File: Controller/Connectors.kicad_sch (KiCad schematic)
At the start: 24 parts, among them J10 Servo, J11 Servo, J12 Thruster, J14 I2C, J15 I2C, J16 UART1, J17 UART2, J18 SPI1, J19 SPI2, J20 Interrupt, J21 Interrupt, J22 Interrupt, J4 Servo, J5 Servo, J6 Servo, J7 Servo, J8 Servo, J9 Servo

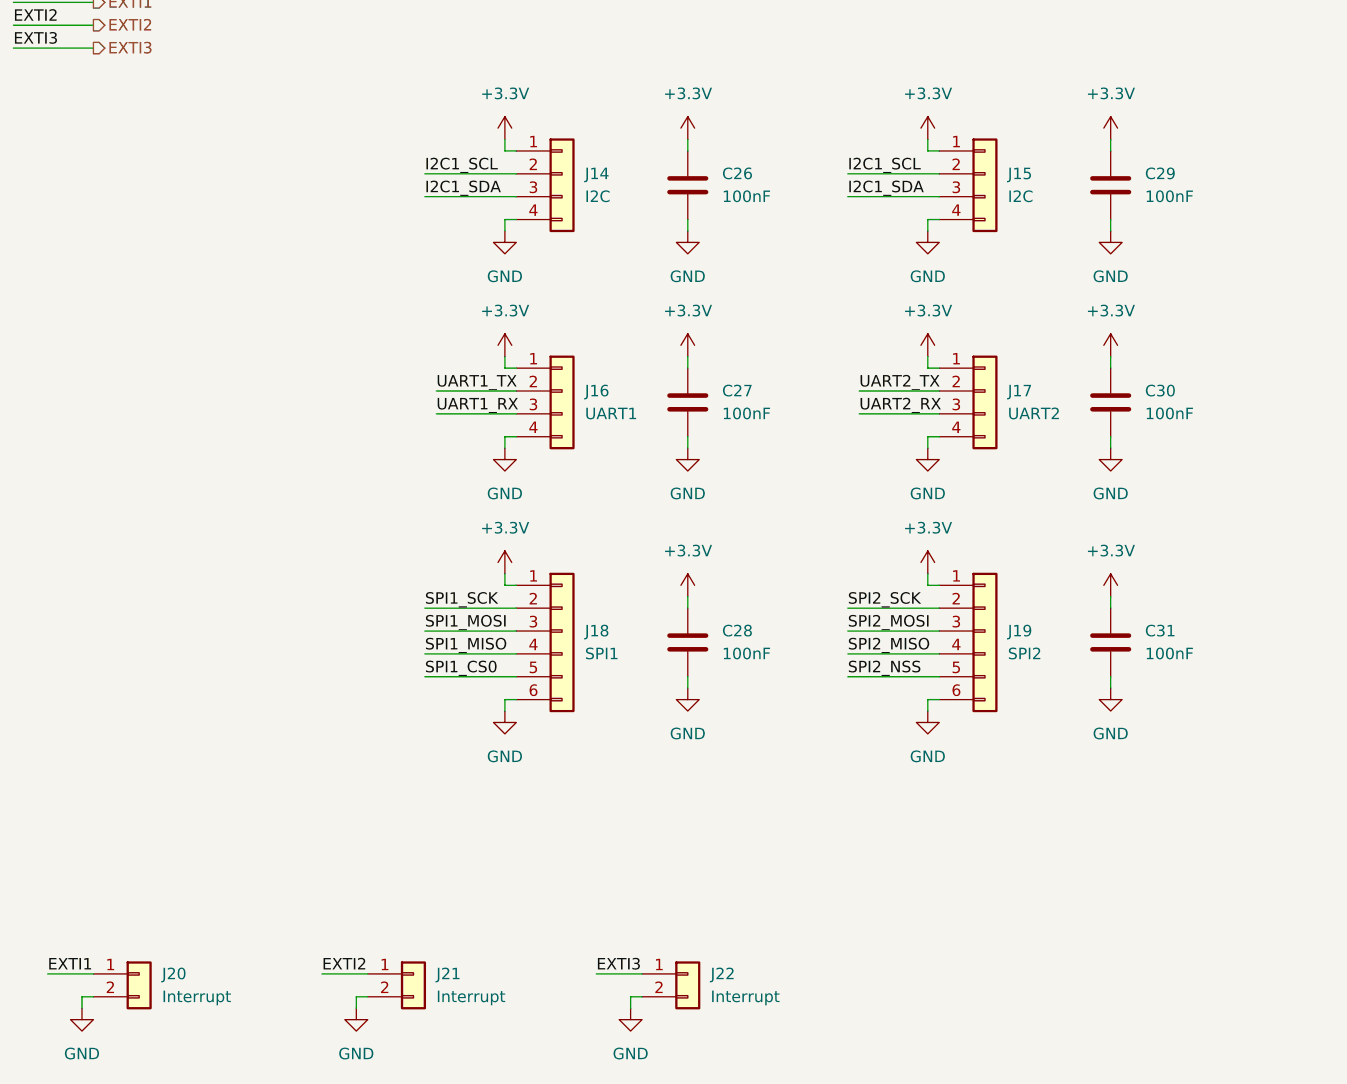
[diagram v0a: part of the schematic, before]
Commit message: Re-number components in controller schematic
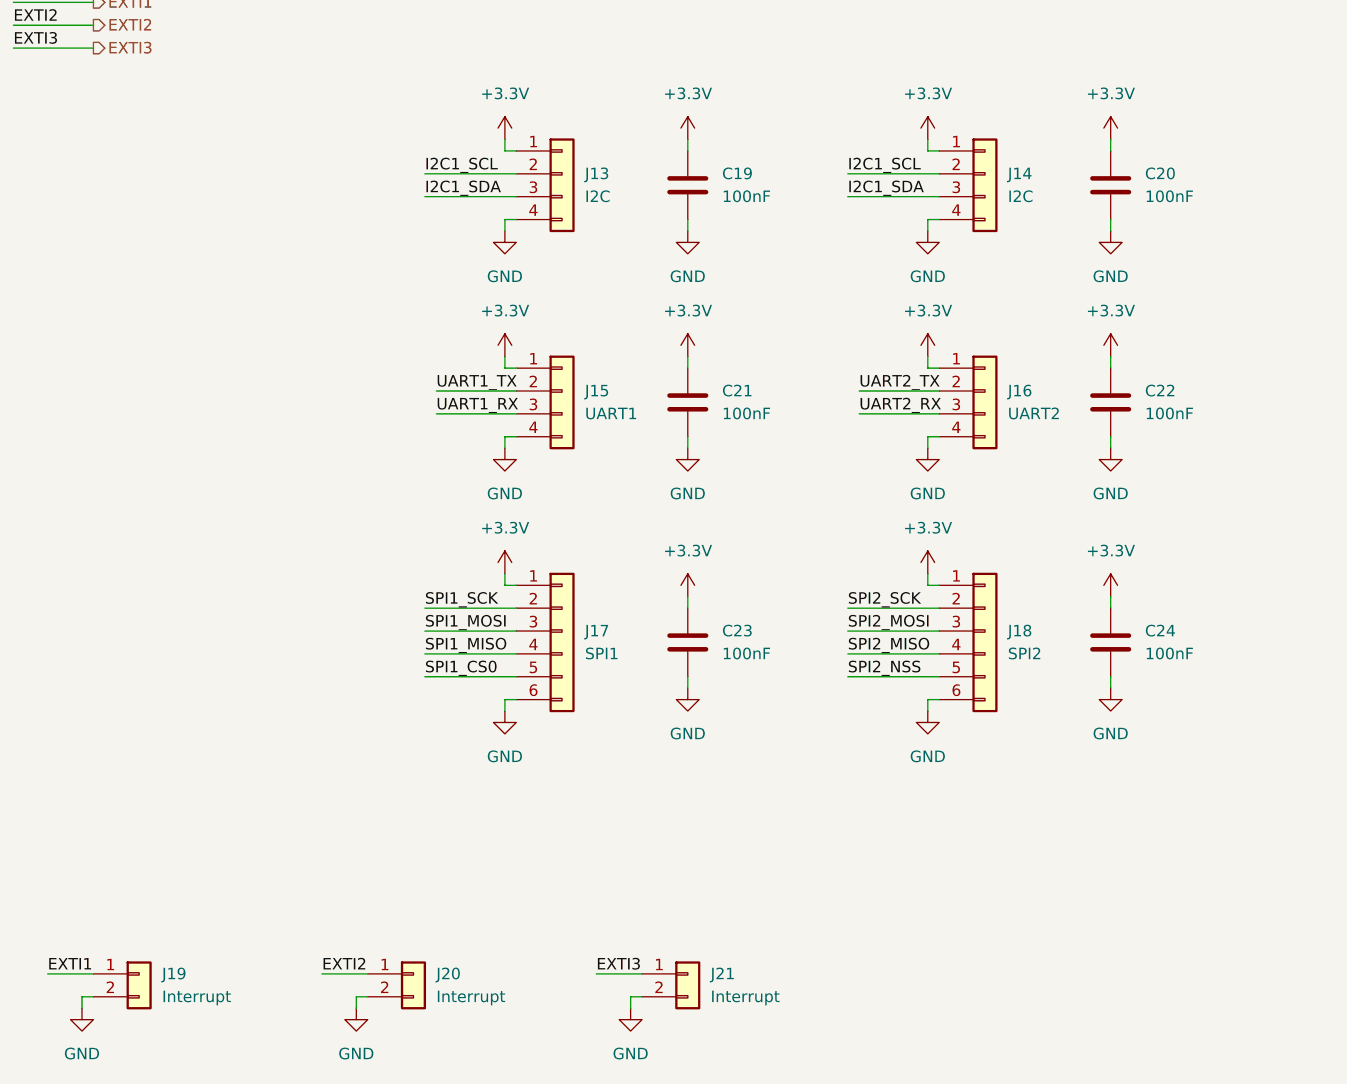
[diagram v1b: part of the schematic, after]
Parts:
- renumbered C26 to C19, C29 to C20, C27 to C21, C30 to C22, C28 to C23, C31 to C24, J14 to J13, J15 to J14, J16 to J15, J17 to J16, J18 to J17, J19 to J18, J20 to J19, J21 to J20, J22 to J21

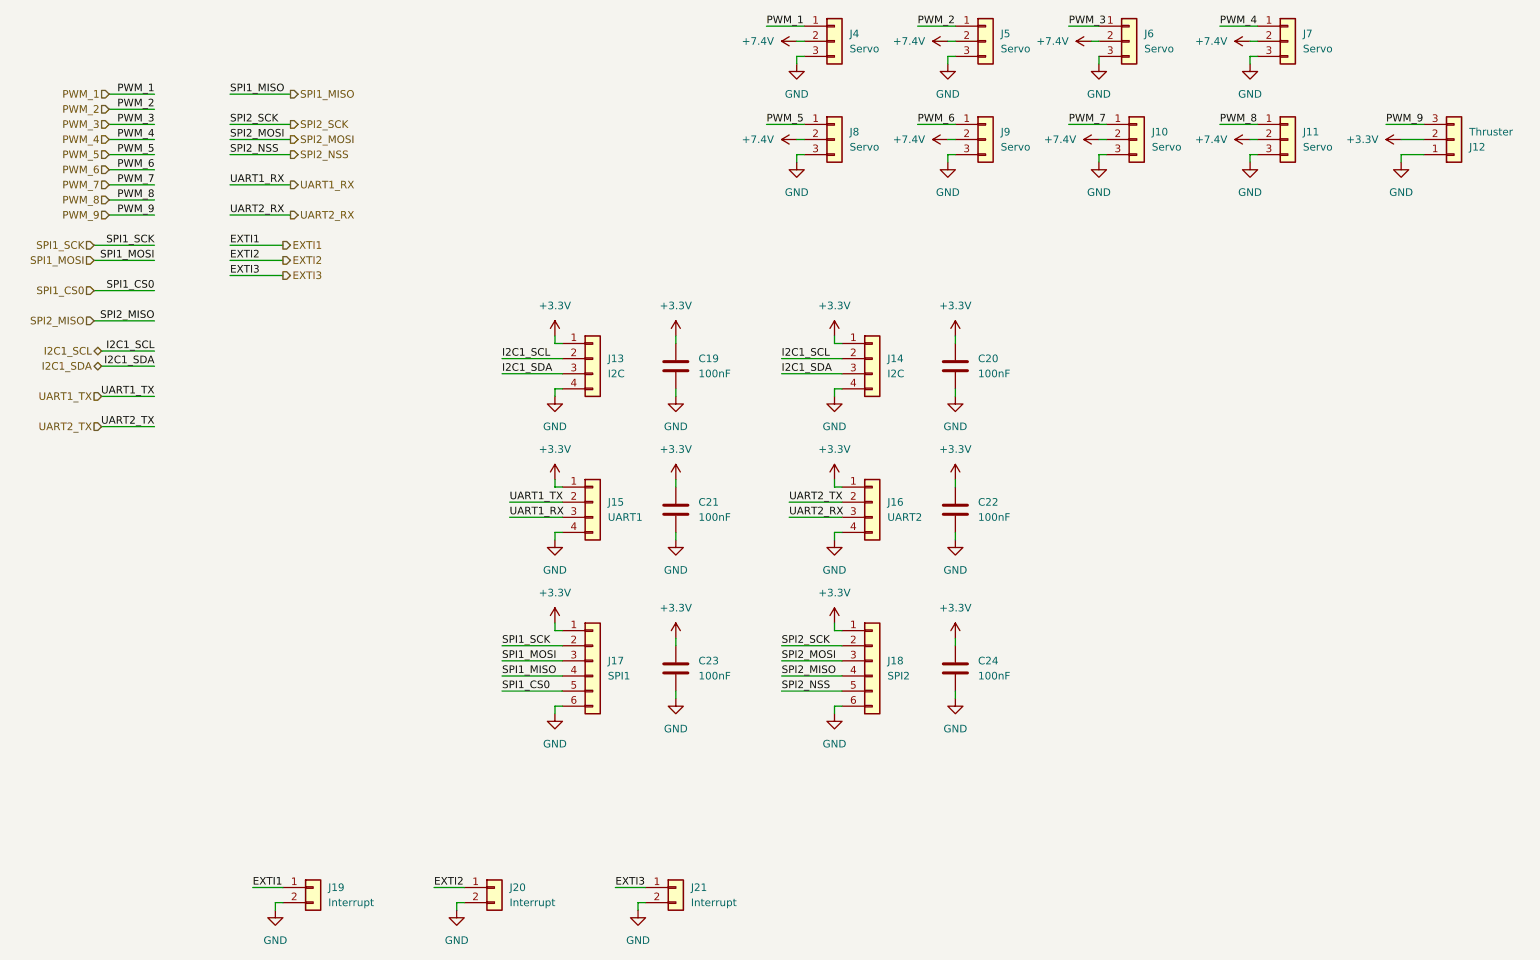
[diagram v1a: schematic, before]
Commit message: Add power input connector to controller schematic
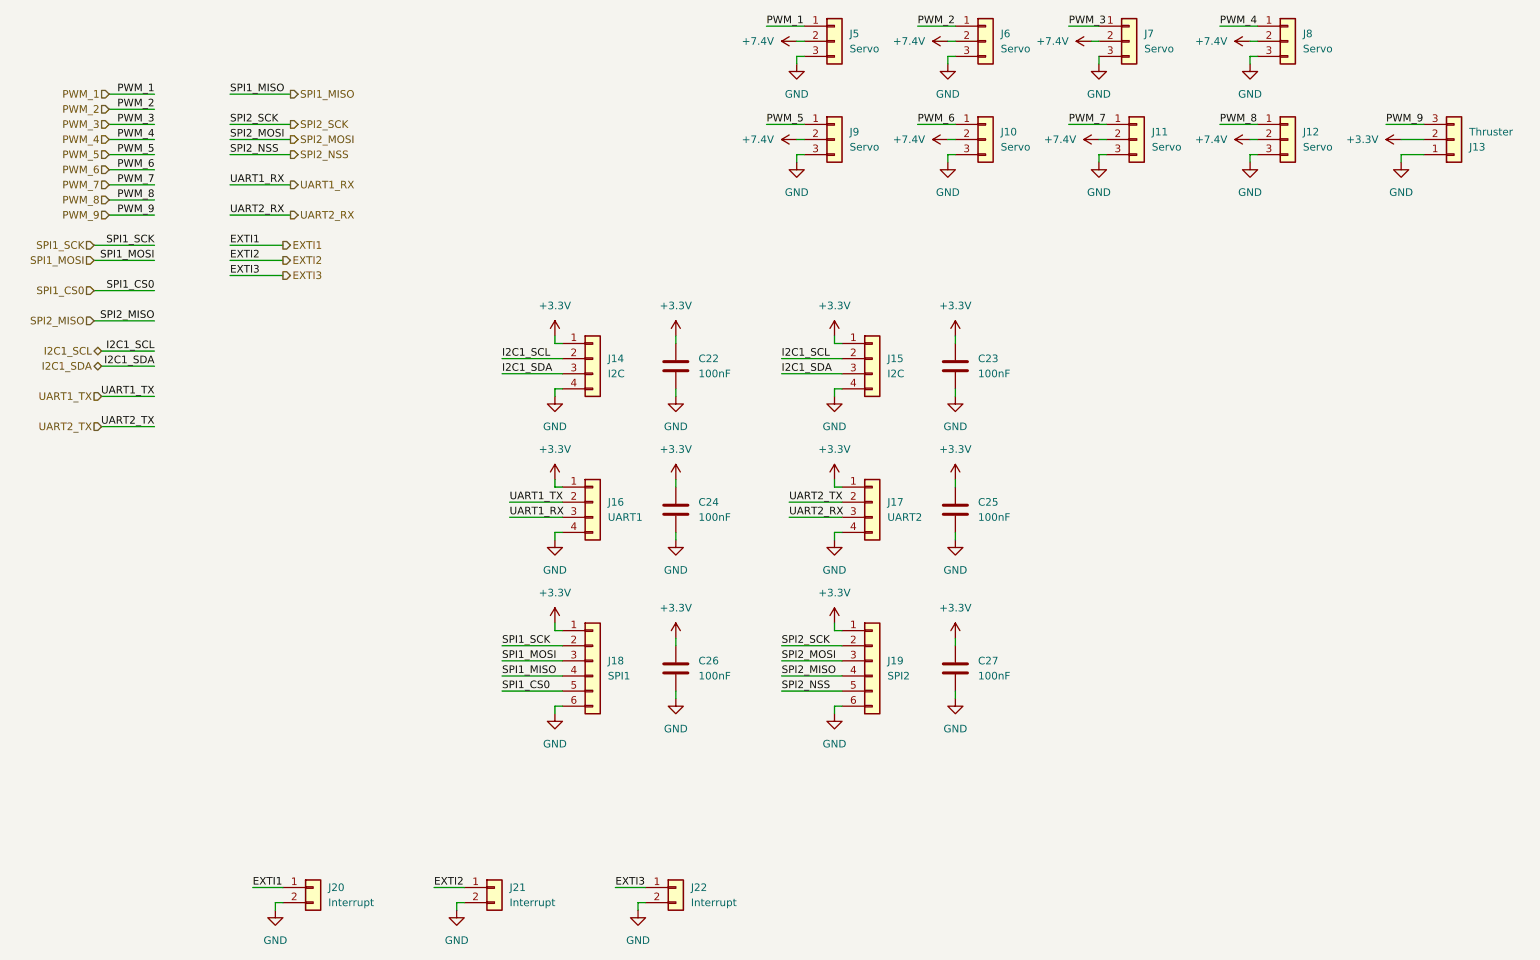
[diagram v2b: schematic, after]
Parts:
- renumbered C19 to C22, C20 to C23, C21 to C24, C22 to C25, C23 to C26, C24 to C27, J9 to J10, J10 to J11, J11 to J12, J12 to J13, J13 to J14, J14 to J15, J15 to J16, J16 to J17, J17 to J18, J18 to J19, J19 to J20, J20 to J21, J21 to J22, J4 to J5, J5 to J6, J6 to J7, J7 to J8, J8 to J9
